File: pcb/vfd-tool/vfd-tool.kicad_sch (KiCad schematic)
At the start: 161 parts, among them J1 Micro_SD_Card, J2 Conn_02x03_Top_Bottom, J3 Conn_02x15_Odd_Even, J4 Raspberry_Pi_2_3, J5 USB_C_Receptacle_USB2.0, J6 Conn_02x15_Odd_Even, SW1 SW_Push, SW2 SW_Push, U1 RP2040, U10 TPS54331DR, U11 PCF85263AT, U2 W25Q32JVSS, U3 TPS562200, U4 TPS562200, U5 FUSB302BMPX, U6 BQ24075RGT, U7 MAX17048G_T10, U8 USB2514B_M2, U9 SRV05-4, Y1 Crystal_GND24, Y2 32.768kHz, Y3 Crystal_GND24

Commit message: assigned footprints to most of the passives
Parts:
- C14, C15, C16, C17, C19, C20, C21, C22, C24, C25, C51: footprint Capacitor_SMD:C_0402_1005Metric_Pad0.74x0.62mm_HandSolder -> Capacitor_SMD:C_0603_1608Metric
- C31: footprint Capacitor_SMD:C_0603_1608Metric -> Capacitor_SMD:C_0402_1005Metric_Pad0.74x0.62mm_HandSolder
- C40, C42: footprint (none) -> Capacitor_SMD:C_0402_1005Metric_Pad0.74x0.62mm_HandSolder
- C44: footprint (none) -> Capacitor_SMD:C_0805_2012Metric
- C46: footprint (none) -> Capacitor_SMD:C_0603_1608Metric
- C47, C48: footprint (none) -> Capacitor_SMD:C_0402_1005Metric
- C49, C50: footprint Capacitor_SMD:C_0603_1608Metric -> Capacitor_SMD:C_0805_2012Metric
- C55, C57: footprint Capacitor_SMD:C_0402_1005Metric_Pad0.74x0.62mm_HandSolder -> Capacitor_SMD:C_0805_2012Metric
- R15, R16, R36, R39, R40, R41, R42, R43, R44, R45, R46, R47, R48, R49, R50: footprint (none) -> Resistor_SMD:R_0402_1005Metric_Pad0.72x0.64mm_HandSolder
- R23, R24: footprint Resistor_SMD:R_0603_1608Metric -> Resistor_SMD:R_0402_1005Metric
- R38: footprint Resistor_SMD:R_0603_1608Metric -> Resistor_SMD:R_0402_1005Metric_Pad0.72x0.64mm_HandSolder
- Y1: value Crystal_GND24 -> 24MHz
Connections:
- net RP2040_GPIO13 is gone; now on net RP2040_CE: U1.16 (GPIO13)
- net GND: now also J6.13 (Pin_13), J6.14 (Pin_14), J6.21 (Pin_21), J6.22 (Pin_22), J6.29 (Pin_29), J6.30 (Pin_30)
- net RPI0_GPIO5: now reaches J6.10 (Pin_10)
- net RPI0_GPIO5: now also J4.29 (GCLK1/GPIO5)
- net RPI0_GPIO7: now reaches J6.11 (Pin_11)
- net RPI0_GPIO7: now also J4.26 (~{CE1}/GPIO7)
- net RPI0_GPIO6: now reaches J6.12 (Pin_12)
- net RPI0_GPIO6: now also J4.31 (GCLK2/GPIO6)
- net RPI0_GPIO12: now reaches J6.15 (Pin_15)
- net RPI0_GPIO12: now also J4.32 (PWM0/GPIO12)
- net RPI0_GPIO16: now reaches J6.16 (Pin_16)
- net RPI0_GPIO16: now also J4.36 (GPIO16)
- net RPI0_GPIO13: now reaches J6.17 (Pin_17)
- net RPI0_GPIO13: now also J4.33 (PWM1/GPIO13)
- net RPI0_GPIO15: now reaches J6.18 (Pin_18)
- net RPI0_GPIO15: now also J4.10 (GPIO15/RXD)
- net RPI0_GPIO14: now reaches J6.19 (Pin_19)
- net RPI0_GPIO14: now also J4.8 (GPIO14/TXD)
- net RPI0_GPIO17: now reaches J6.20 (Pin_20)
- net RPI0_GPIO17: now also J4.11 (GPIO17)
- net RPI0_GPIO18: now reaches J6.23 (Pin_23)
- net RPI0_GPIO18: now also J4.12 (GPIO18/PWM0)
- net RPI0_GPIO21: now reaches J6.24 (Pin_24)
- net RPI0_GPIO21: now also J4.40 (GPIO21/SCLK1)
- net RPI0_GPIO19: now reaches J6.25 (Pin_25)
- net RPI0_GPIO19: now also J4.35 (GPIO19/MISO1)
- net RPI0_GPIO22: now reaches J6.26 (Pin_26)
- net RPI0_GPIO22: now also J4.15 (GPIO22)
- net RPI0_GPIO20: now reaches J6.27 (Pin_27)
- net RPI0_GPIO20: now also J4.38 (GPIO20/MOSI1)
- net RPI0_GPIO23: now reaches J6.28 (Pin_28)
- net RPI0_GPIO23: now also J4.16 (GPIO23)
- net RPI0_GPIO0: now reaches J6.7 (Pin_7)
- net RPI0_GPIO0: now also J4.27 (ID_SD/GPIO0)
- net RPI0_GPIO4: now reaches J6.8 (Pin_8)
- net RPI0_GPIO4: now also J4.7 (GCLK0/GPIO4)
- net RPI0_GPIO1: now reaches J6.9 (Pin_9)
- net RPI0_GPIO1: now also J4.28 (ID_SC/GPIO1)
- net RPI0_GPIO27: now reaches J4.13 (GPIO27)
- net RPI0_GPIO24: now reaches J4.18 (GPIO24)
- net RPI0_GPIO25: now reaches J4.22 (GPIO25)
- net RPI0_GPIO26: now reaches J4.37 (GPIO26)
- net RP2040_GPIO18 renamed BATT_INT
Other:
- moved on the sheet: D2, J4, J6, TP1, TP2

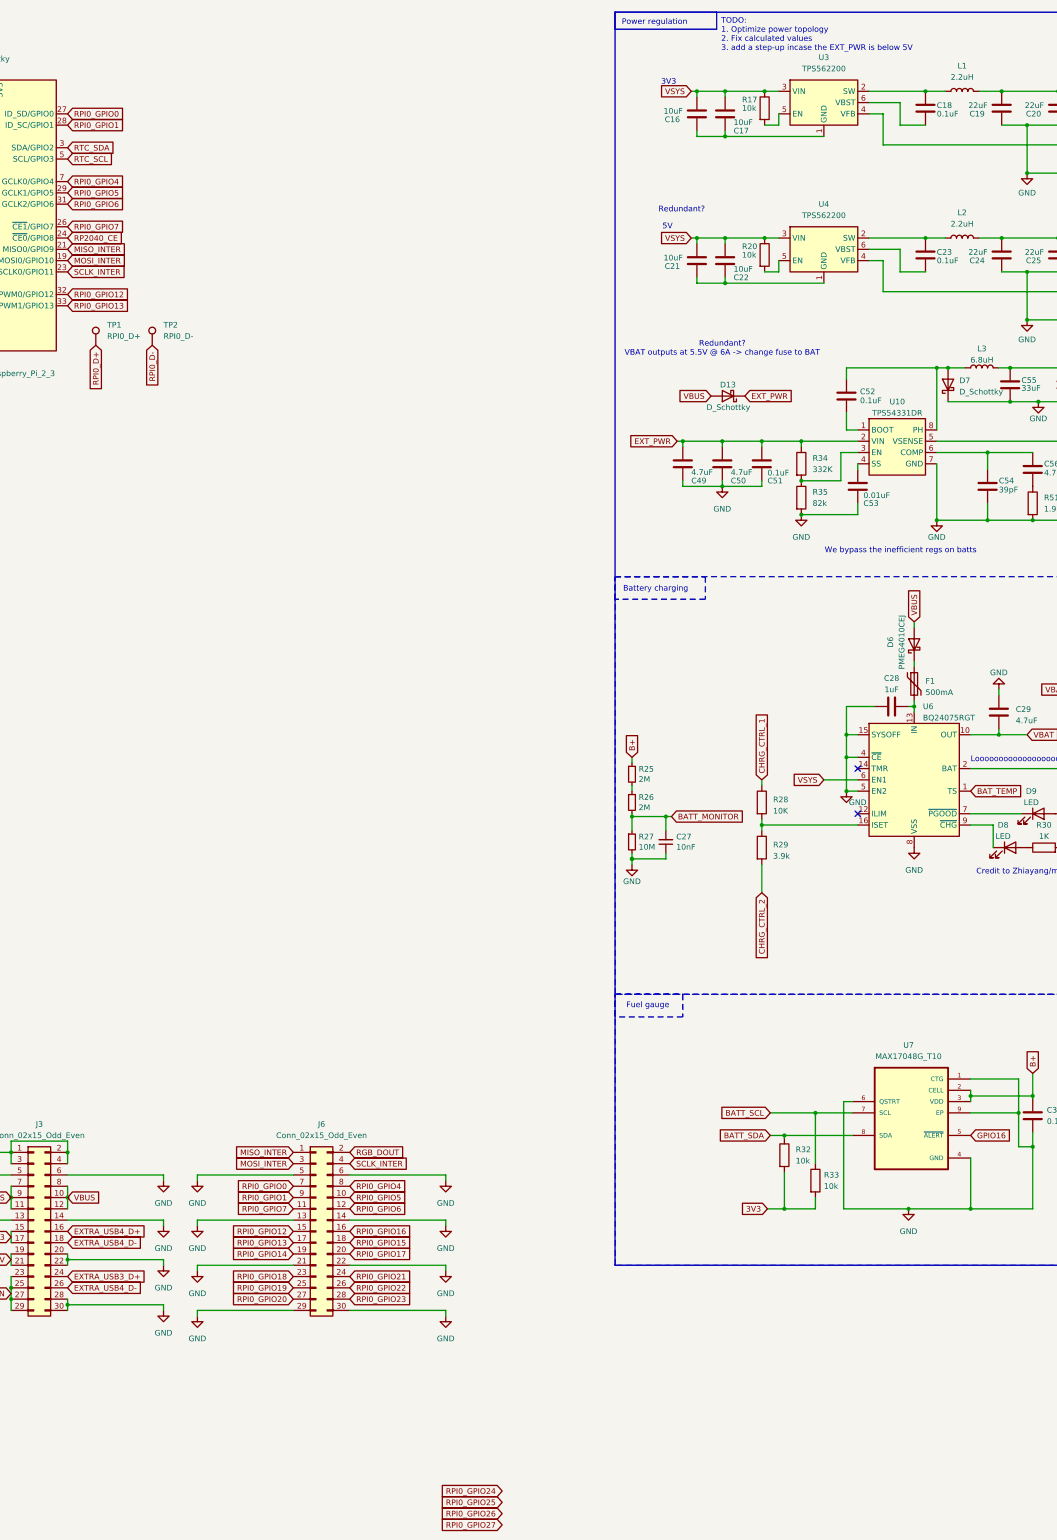
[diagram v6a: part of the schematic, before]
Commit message: recalculated values for the regulators and found LCSC components for most of the symbols
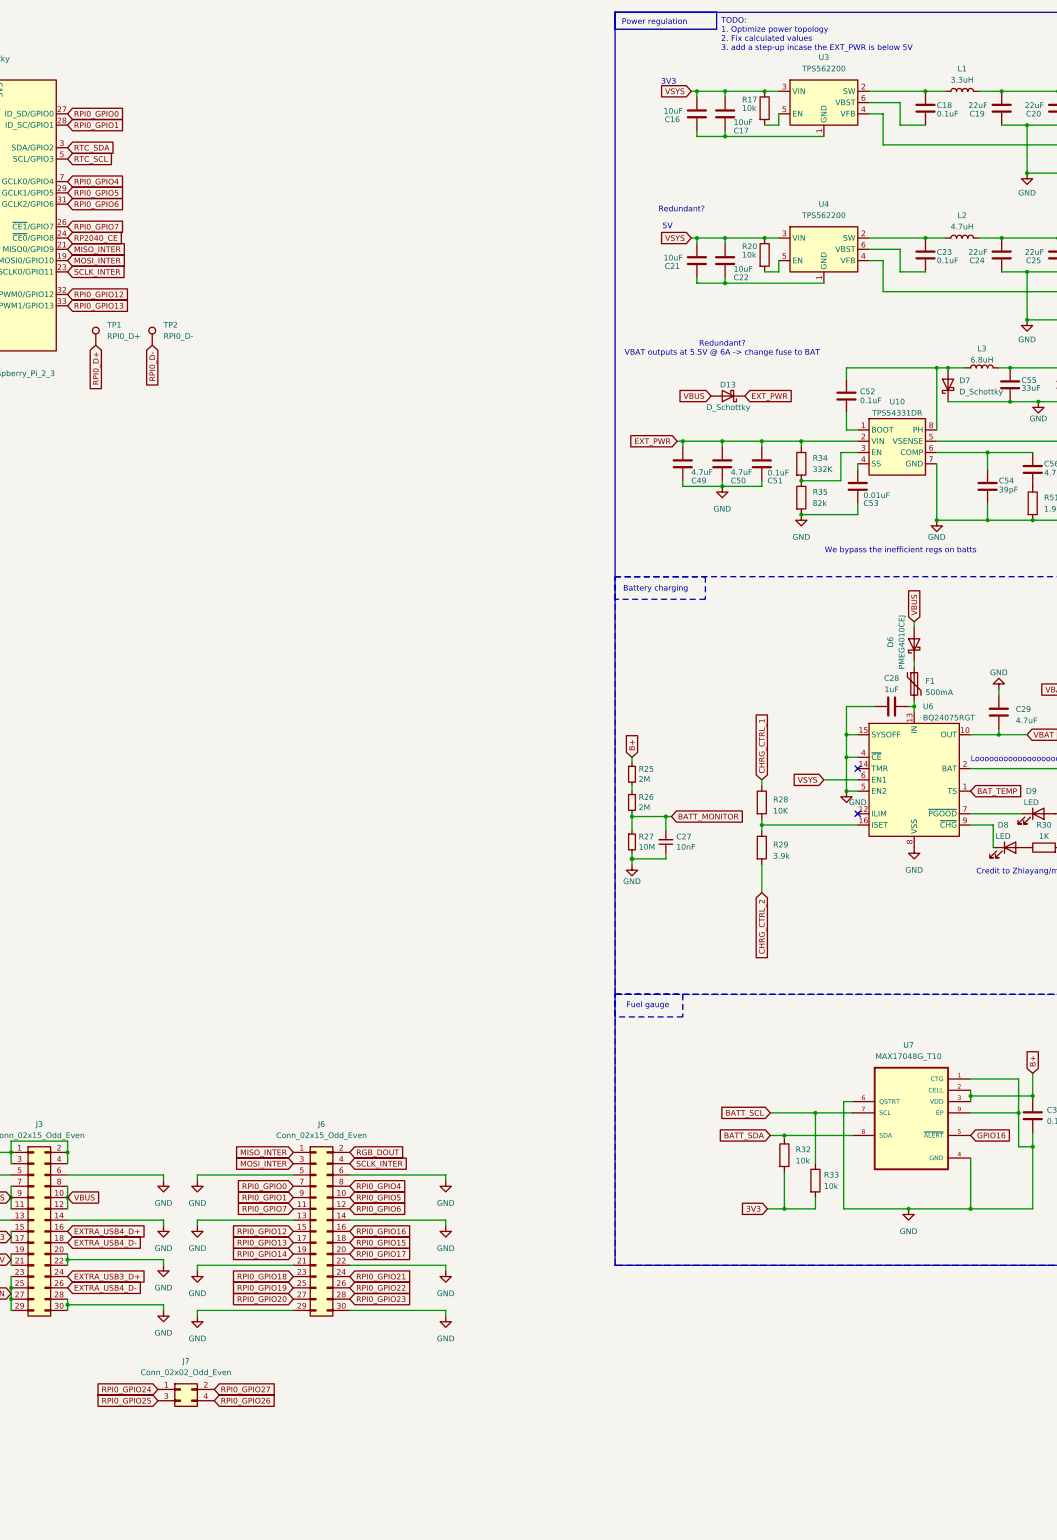
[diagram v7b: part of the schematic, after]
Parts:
- added J7: Conn_02x02_Odd_Even, symbol Connector_Generic:Conn_02x02_Odd_Even
- BT1: footprint (none) -> CR2032-BS-6-1:BAT_CR2032-BS-6-1
- L1: value 2.2uH -> 3.3uH; footprint Inductor_SMD:L_0805_2012Metric_Pad1.05x1.20mm_HandSolder -> Inductor_SMD:L_Chilisin_BMRB00060612
- L2: value 2.2uH -> 4.7uH; footprint Inductor_SMD:L_0805_2012Metric_Pad1.05x1.20mm_HandSolder -> Inductor_SMD:L_Chilisin_BMRB00060612
- L3: footprint (none) -> Inductor_SMD:L_Chilisin_BMRB00060612
- SW1, SW2: footprint footprints:SW_TS-1187A-B-A-B -> Button_Switch_SMD:SW_SPST_B3U-1000P
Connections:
- net RPI0_GPIO24: now also J7.1 (Pin_1)
- net RPI0_GPIO25: now also J7.3 (Pin_3)
- net RPI0_GPIO26: now also J7.4 (Pin_4)
- net RPI0_GPIO27: now also J7.2 (Pin_2)
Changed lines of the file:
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@@
 	(global_label "RPI0_GPIO26"
 		(shape input)
-		(at 426.72 353.06 180)
+		(at 361.95 327.66 0)
 		(fields_autoplaced yes)
 		(effects
@@
 				(size 1.27 1.27)
 			)
-			(justify right)
+			(justify left)
 		)
 		(property "Intersheetrefs" "${INTERSHEET_REFS}"
-			(at 411.5186 353.06 0)
+			(at 377.1514 327.66 0)
 			(effects
 				(font
 					(size 1.27 1.27)
 				)
-				(justify right)
+				(justify left)
 				(hide yes)
 			)
@@
 	(global_label "RPI0_GPIO24"
 		(shape input)
-		(at 426.72 347.98 180)
+		(at 349.25 325.12 180)
 		(fields_autoplaced yes)
 		(effects
@@
 		)
 		(property "Intersheetrefs" "${INTERSHEET_REFS}"
-			(at 411.5186 347.98 0)
+			(at 334.0486 325.12 0)
 			(effects
 				(font
@@
 	(global_label "RPI0_GPIO25"
 		(shape input)
-		(at 426.72 350.52 180)
+		(at 349.25 327.66 180)
 		(fields_autoplaced yes)
 		(effects
@@
 		)
 		(property "Intersheetrefs" "${INTERSHEET_REFS}"
-			(at 411.5186 350.52 0)
+			(at 334.0486 327.66 0)
 			(effects
 				(font
@@
 	(global_label "RPI0_GPIO27"
 		(shape input)
-		(at 426.72 355.6 180)
+		(at 361.95 325.12 0)
 		(fields_autoplaced yes)
 		(effects
@@
 				(size 1.27 1.27)
 			)
-			(justify right)
+			(justify left)
 		)
 		(property "Intersheetrefs" "${INTERSHEET_REFS}"
-			(at 411.5186 355.6 0)
+			(at 377.1514 325.12 0)
 			(effects
 				(font
 					(size 1.27 1.27)
 				)
-				(justify right)
+				(justify left)
 				(hide yes)
 			)
@@
 			)
 		)
-		(property "Footprint" ""
+		(property "Footprint" "CR2032-BS-6-1:BAT_CR2032-BS-6-1"
 			(at 241.3 37.846 90)
 			(effects
@@
 			)
 		)
-		(property "Description" "Single-cell battery"
+		(property "Description" "C70377"
 			(at 241.3 39.37 0)
 			(effects
@@
 			)
 		)
-		(property "Description" ""
+		(property "Description" "C220679"
 			(at 99.06 271.78 0)
 			(effects
@@
 			)
 		)
-		(property "Footprint" ""
+		(property "Footprint" "Inductor_SMD:L_Chilisin_BMRB00060612"
 			(at 534.67 95.25 0)
 			(effects
@@
 			)
 		)
-		(property "Description" "Inductor"
+		(property "Description" "C5189749"
 			(at 534.67 95.25 0)
 			(effects
@@
 			)
 		)
-		(property "Description" ""
+		(property "Description" "C49757"
 			(at 499.11 35.56 0)
 			(effects
@@
 			)
 		)
-		(property "Footprint" "footprints:SW_TS-1187A-B-A-B"
+		(property "Footprint" "Button_Switch_SMD:SW_SPST_B3U-1000P"
 			(at 33.02 175.26 0)
 			(effects
@@
 			)
 		)
-		(property "Footprint" "footprints:SW_TS-1187A-B-A-B"
+		(property "Footprint" "Button_Switch_SMD:SW_SPST_B3U-1000P"
 			(at 55.88 175.26 0)
 			(effects
@@
 			)
 		)
-		(property "Description" ""
+		(property "Description" "C49757"
 			(at 499.11 68.58 0)
 			(effects
@@
 			)
 		)
-		(property "Description" ""
+		(property "Description" "C15464"
 			(at 519.43 187.96 0)
 			(effects
@@
 			)
 		)
-		(property "Description" ""
+		(property "Description" "C9865"
 			(at 514.35 105.41 0)
 			(effects
@@
 		(fields_autoplaced yes)
 		(property "Reference" "L2"
-			(at 530.225 60.325 90)
+			(at 530.225 60.96 90)
 			(effects
 				(font
@@
 			)
 		)
-		(property "Value" "2.2uH"
-			(at 530.225 62.865 90)
+		(property "Value" "4.7uH"
+			(at 530.225 63.5 90)
 			(effects
 				(font
@@
 			)
 		)
-		(property "Footprint" "Inductor_SMD:L_0805_2012Metric_Pad1.05x1.20mm_HandSolder"
+		(property "Footprint" "Inductor_SMD:L_Chilisin_BMRB00060612"
 			(at 530.225 66.04 0)
 			(effects
@@
 			)
 		)
-		(property "Description" ""
+		(property "Description" "C5189748"
 			(at 530.225 66.04 0)
 			(effects
@@
 		(fields_autoplaced yes)
 		(property "Reference" "L1"
-			(at 530.225 27.305 90)
+			(at 530.225 27.94 90)
 			(effects
 				(font
@@
 			)
 		)
-		(property "Value" "2.2uH"
-			(at 530.225 29.845 90)
+		(property "Value" "3.3uH"
+			(at 530.225 30.48 90)
 			(effects
 				(font
@@
 			)
 		)
-		(property "Footprint" "Inductor_SMD:L_0805_2012Metric_Pad1.05x1.20mm_HandSolder"
+		(property "Footprint" "Inductor_SMD:L_Chilisin_BMRB00060612"
 			(at 530.225 33.02 0)
 			(effects
@@
 			)
 		)
-		(property "Description" ""
+		(property "Description" "C5189747"
 			(at 530.225 33.02 0)
 			(effects
@@
 					(unit 1)
 				)
+			)
+		)
+	)
+	(symbol
+		(lib_id "Connector_Generic:Conn_02x02_Odd_Even")
+		(at 354.33 325.12 0)
+		(unit 1)
+		(exclude_from_sim no)
+		(in_bom yes)
+		(on_board yes)
+		(dnp no)
+		(fields_autoplaced yes)
+		(property "Reference" "J7"
+			(at 355.6 318.77 0)
+			(effects
+				(font
+					(size 1.27 1.27)
+				)
+			)
+		)
+		(property "Value" "Conn_02x02_Odd_Even"
+			(at 355.6 321.31 0)
+			(effects
+				(font
+					(size 1.27 1.27)
+				)
+			)
+		)
+		(property "Footprint" ""
+			(at 354.33 325.12 0)
+			(effects
+				(font
+					(size 1.27 1.27)
+				)
+				(hide yes)
+			)
+		)
+		(property "Datasheet" "~"
+			(at 354.33 325.12 0)
+			(effects
+				(font
+					(size 1.27 1.27)
+				)
+				(hide yes)
+			)
+		)
+		(property "Description" "Generic connector, double row, 02x02, odd/even pin numbering scheme (row 1 odd numbers, row 2 even numbers), script generated (kicad-library-utils/schlib/autogen/connector/)"
+			(at 354.33 325.12 0)
+			(effects
+				(font
+					(size 1.27 1.27)
+				)
+				(hide yes)
+			)
+		)
+		(pin "1"
+		)
+		(pin "3"
+		)
+		(pin "4"
+		)
+		(pin "2"
+		)
+		(instances
+			(project "vfd-tool"
+				(path "/849d9919-4175-4212-8785-6cd0421cfa2d"
+					(reference "J7")
+					(unit 1)
+				)

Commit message: Fixed footprints
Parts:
- removed D7: D_Schottky, symbol Device:D_Schottky
- removed J2: Conn_02x03_Top_Bottom, symbol Connector_Generic:Conn_02x03_Top_Bottom
- removed J7: Conn_02x02_Odd_Even, symbol Connector_Generic:Conn_02x02_Odd_Even
- added D15: CMS04, Diode_SMD:D_SOD-128, symbol Device:D_Schottky
- added J2: Conn_ARM_SWD_TagConnect_TC2030-NL, Paw-Connect:Paw-Connect_RevA_TC2030-IDC-NL_2x03_P1.27mm_Vertical, symbol Connector:Conn_ARM_SWD_TagConnect_TC2030-NL
- added J7: Conn_02x08_Odd_Even, Connector_PinHeader_1.27mm:PinHeader_2x08_P1.27mm_Vertical, symbol Connector_Generic:Conn_02x08_Odd_Even
- added R57: 1k, Resistor_SMD:R_0402_1005Metric, symbol Device:R
- C1, C2, C34, C35: value 30pF -> 14pF
- C32, R34, R35, R51, R52, R53: footprint (none) -> Resistor_SMD:R_0402_1005Metric
- C58, C59: footprint (none) -> Capacitor_SMD:C_0402_1005Metric
- D10, D13, D2: value D_Schottky -> CMS04; footprint (none) -> Diode_SMD:D_SOD-128
- D11: footprint (none) -> Diode_SMD:D_SOD-323
- D12, D14: value D_Schottky -> SS84; footprint (none) -> Diode_SMD:D_SMC
- J3, J6: footprint (none) -> Connector_PinHeader_1.27mm:PinHeader_2x15_P1.27mm_Vertical
- J4: footprint (none) -> ADA3708:MODULE_ADA3708
- JP1: footprint Connector_PinHeader_1.00mm:PinHeader_1x02_P1.00mm_Vertical -> Jumper:SolderJumper-2_P1.3mm_Open_TrianglePad1.0x1.5mm
- TP1, TP2: footprint (none) -> TestPoint:TestPoint_Pad_D3.0mm
- Y1: footprint KiCad:SMD3225_4P12288MHZ12PF10PPM4085 -> Crystal:Crystal_SMD_3225-4Pin_3.2x2.5mm
- Y2: footprint (none) -> Crystal:Crystal_SMD_3215-2Pin_3.2x1.5mm
- Y3: value Crystal_GND24 -> 24MHz; footprint KiCad:SMD3225_4P12288MHZ12PF10PPM4085 -> Crystal:Crystal_SMD_3225-4Pin_3.2x2.5mm
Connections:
- net 3V3: now also J2.1 (VCC), R57.1
- net EXT_PWR: now also D12.1 (K); no longer D13.1 (K)
- net GND: now also D13.1 (K), J2.5 (GND), J7.10 (Pin_10), J7.13 (Pin_13), J7.5 (Pin_5), J7.6 (Pin_6), J7.8 (Pin_8)
- net RP2040_GPIO10: now also J7.9 (Pin_9)
- net RP2040_GPIO11: now also J7.7 (Pin_7)
- net RP2040_GPIO12: now also J7.11 (Pin_11)
- net RPI0_GPIO24: now also J7.1 (Pin_1)
- net RPI0_GPIO25: now also J7.3 (Pin_3)
- net RPI0_GPIO26: now also J7.4 (Pin_4)
- net RPI0_GPIO27: now also J7.2 (Pin_2)
- net RUN: now also J2.3 (~{RESET})
- net SWCLK_RP2040: now also J2.4 (SWCLK)
- net SWD_RP2040: now also J2.2 (SWDIO)
- net VBUS: now also D12.2 (A); no longer D13.2 (A)
- net VSYS: now also D15.1 (K); no longer D12.1 (K)
- net at C52.1, L3.1, U10.8 (PH): now also D13.2 (A)
- net at C55.1, C57.1, L3.2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: now also D15.2 (A); no longer D12.2 (A)
- net RP2040_GPIO27: now reaches U1.39 (GPIO27_ADC1)
- net RP2040_GPIO27: now also J7.12 (Pin_12)
- net RP2040_GPIO28: now reaches U1.40 (GPIO28_ADC2)
- net RP2040_GPIO28: now also J7.14 (Pin_14)
- net RP2040_GPIO29: now reaches U1.41 (GPIO29_ADC3)
- net RP2040_GPIO29: now also J7.16 (Pin_16)
- net GPIO7 renamed ONEWIRE_DETECT
- net ONEWIRE_DETECT: now also J7.15 (Pin_15), R57.2
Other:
- note added: "C_{L} = 12"
- note added: "C_{L} = 12.5"
- note removed: "Debug REDFIT IDC"
